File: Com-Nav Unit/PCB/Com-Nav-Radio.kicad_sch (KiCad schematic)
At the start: 91 parts, among them J1 USB_C_Receptacle_USB2.0_14P, Q10 SS8550, Q11 SS8550, Q12 SS8550, Q13 SS8550, Q14 SS8550, Q15 SS8550, Q16 SS8550, Q2 SS8550, Q3 SS8550, Q4 SS8550, Q5 SS8550, Q6 SS8550, Q7 SS8550, Q8 SS8550, Q9 SS8550, SW1 EC12D1524403, SW10 SW_Push, SW2 EC12E1240301, SW3 EC12D1524403, SW4 EC12E1240301, SW7 SW_Push, SW8 SW_Push, SW9 SW_Push, U1 STM32F411CEUx, U2 74HC595, U3 74HC595, U4 XC6206P332MR, Y2 25 MHz

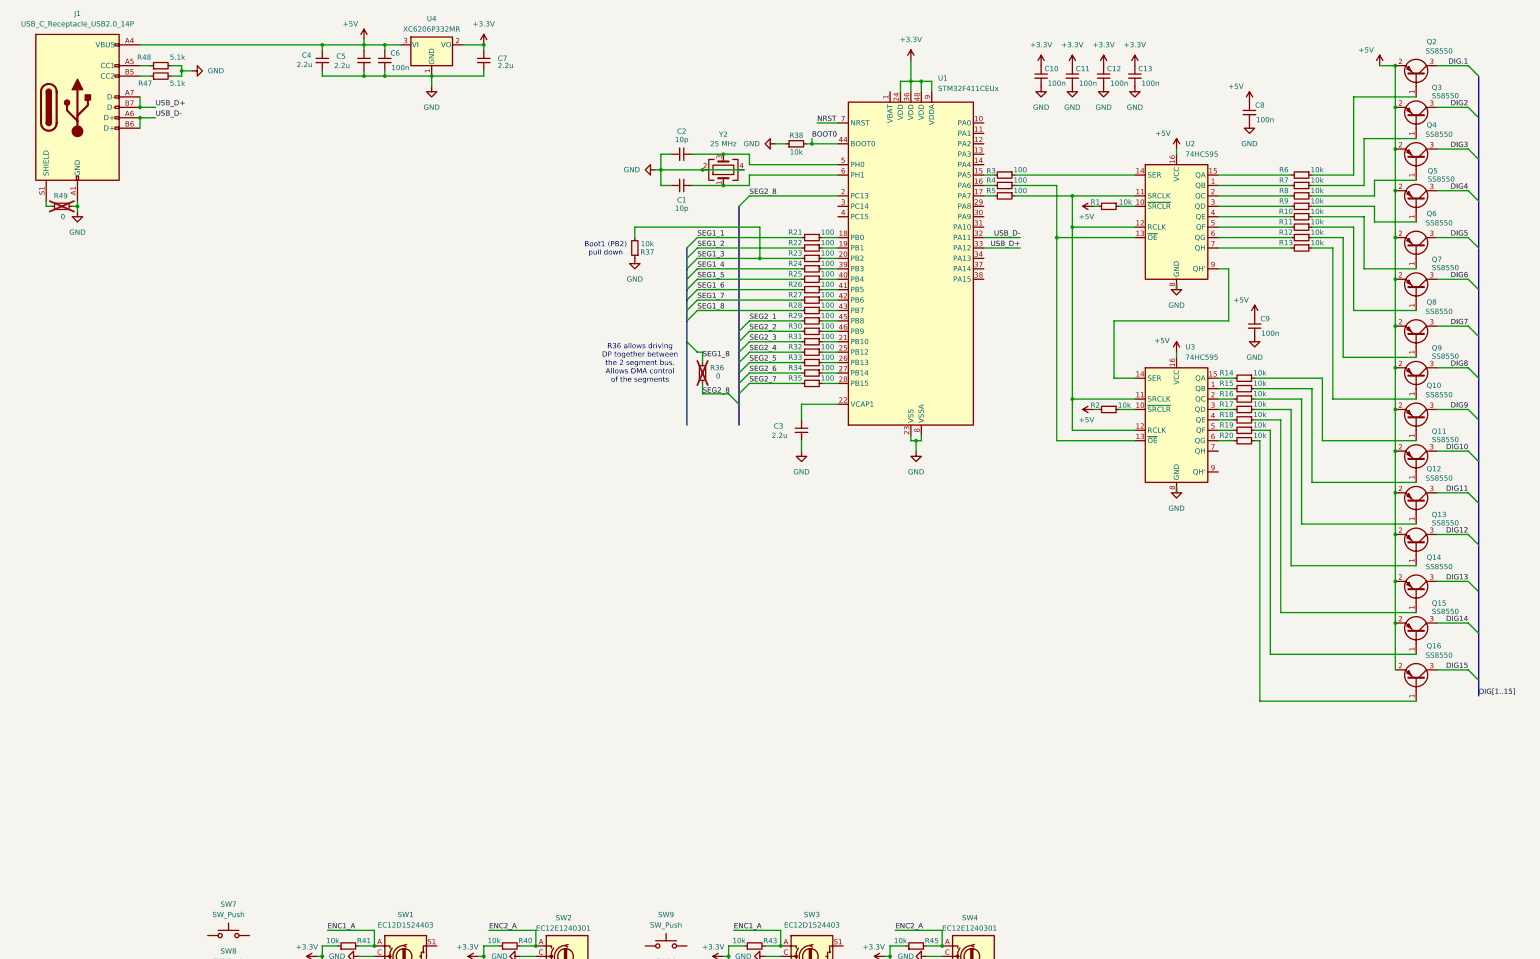
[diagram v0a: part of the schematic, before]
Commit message: PCB- Sch Connect 7 segments
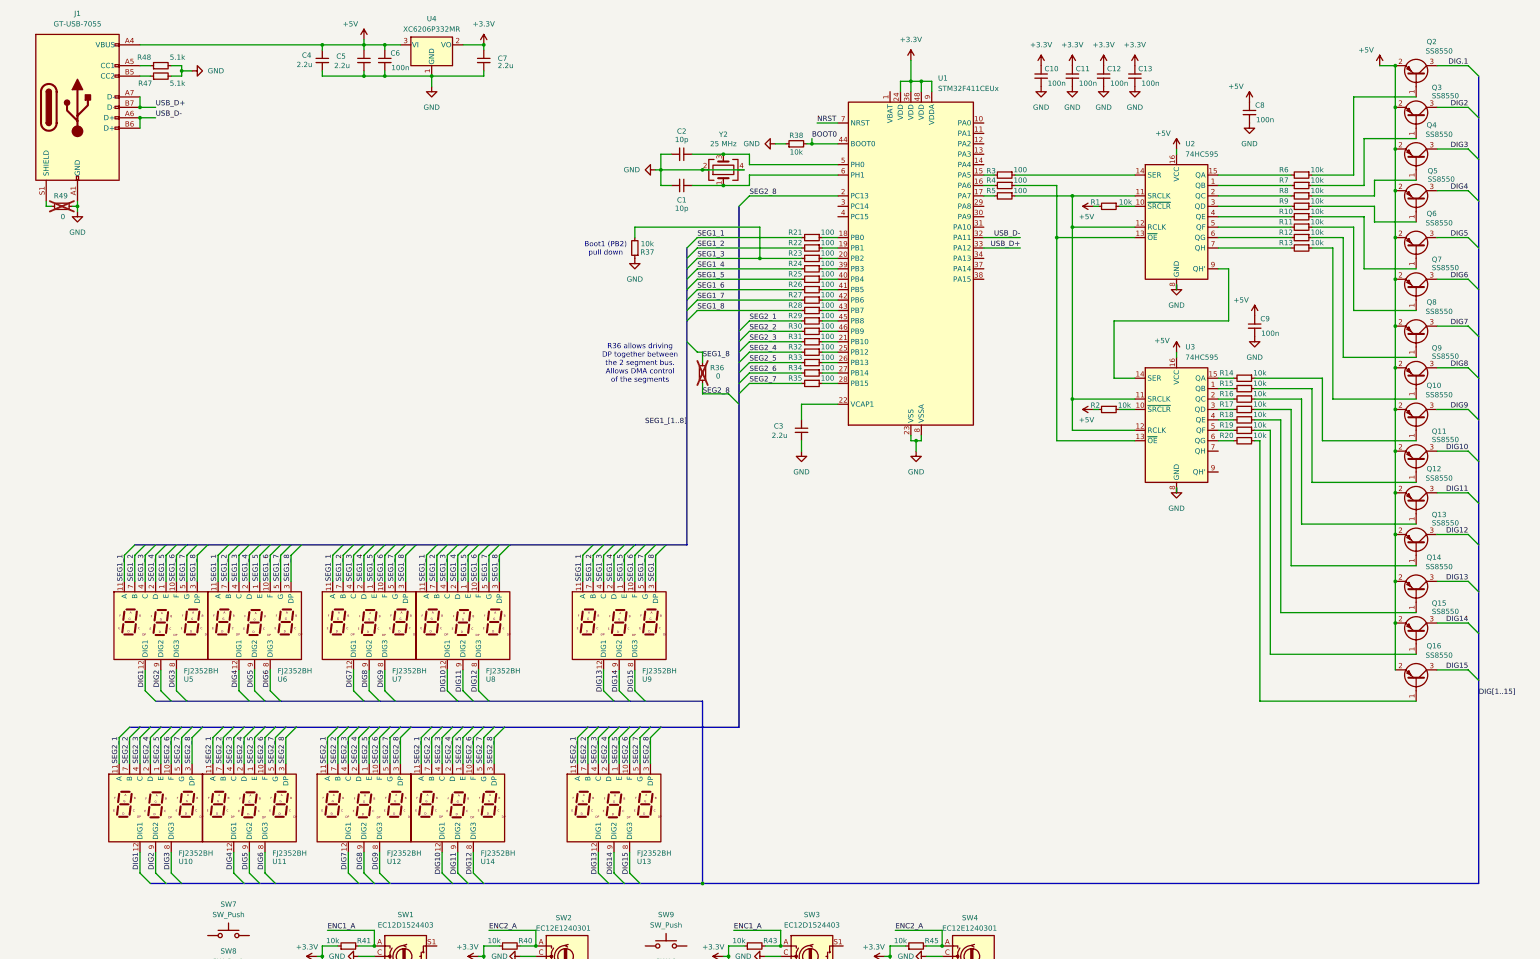
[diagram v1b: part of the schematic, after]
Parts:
- added U10, U11, U12, U13, U14, U5, U6, U7, U8, U9: FJ2352BH, Custom_7seg:FJ2352BH, symbol Custom_7seg:FJ2352BH
- J1: value USB_C_Receptacle_USB2.0_14P -> GT-USB-7055; footprint Connectors:USB_C_Receptacle_G-Switch_GT-USB-7051x -> Connectors:USB_C_Receptacle_G-Switch_GT-USB-7055x; PN (none) -> GT-USB-7055
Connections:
- net DIG10: now also U14.12 (DIG1), U8.12 (DIG1)
- net DIG11: now also U14.9 (DIG2), U8.9 (DIG2)
- net DIG12: now also U14.8 (DIG3), U8.8 (DIG3)
- net DIG13: now also U13.12 (DIG1), U9.12 (DIG1)
- net DIG14: now also U13.9 (DIG2), U9.9 (DIG2)
- net DIG15: now also U13.8 (DIG3), U9.8 (DIG3)
- net DIG2: now also U10.9 (DIG2), U5.9 (DIG2)
- net DIG3: now also U10.8 (DIG3), U5.8 (DIG3)
- net DIG4: now also U11.12 (DIG1), U6.12 (DIG1)
- net DIG5: now also U11.9 (DIG2), U6.9 (DIG2)
- net DIG6: now also U11.8 (DIG3), U6.8 (DIG3)
- net DIG7: now also U12.12 (DIG1), U7.12 (DIG1)
- net DIG8: now also U12.9 (DIG2), U7.9 (DIG2)
- net DIG9: now also U12.8 (DIG3), U7.8 (DIG3)
- net SEG1_1: now also U5.11 (A), U6.11 (A), U7.11 (A), U8.11 (A), U9.11 (A)
- net SEG1_2: now also U5.7 (B), U6.7 (B), U7.7 (B), U8.7 (B), U9.7 (B)
- net SEG1_3: now also U5.4 (C), U6.4 (C), U7.4 (C), U8.4 (C), U9.4 (C)
- net SEG1_4: now also U5.2 (D), U6.2 (D), U7.2 (D), U8.2 (D), U9.2 (D)
- net SEG1_5: now also U5.1 (E), U6.1 (E), U7.1 (E), U8.1 (E), U9.1 (E)
- net SEG1_6: now also U5.10 (F), U6.10 (F), U7.10 (F), U8.10 (F), U9.10 (F)
- net SEG1_7: now also U5.5 (G), U6.5 (G), U7.5 (G), U8.5 (G), U9.5 (G)
- net SEG1_8: now also U5.3 (DP), U6.3 (DP), U7.3 (DP), U8.3 (DP), U9.3 (DP)
- net SEG2_1: now also U10.11 (A), U11.11 (A), U12.11 (A), U13.11 (A), U14.11 (A)
- net SEG2_2: now also U10.7 (B), U11.7 (B), U12.7 (B), U13.7 (B), U14.7 (B)
- net SEG2_3: now also U10.4 (C), U11.4 (C), U12.4 (C), U13.4 (C), U14.4 (C)
- net SEG2_4: now also U10.2 (D), U11.2 (D), U12.2 (D), U13.2 (D), U14.2 (D)
- net SEG2_5: now also U10.1 (E), U11.1 (E), U12.1 (E), U13.1 (E), U14.1 (E)
- net SEG2_6: now also U10.10 (F), U11.10 (F), U12.10 (F), U13.10 (F), U14.10 (F)
- net SEG2_7: now also U10.5 (G), U11.5 (G), U12.5 (G), U13.5 (G), U14.5 (G)
- net SEG2_8: now also U10.3 (DP), U11.3 (DP), U12.3 (DP), U13.3 (DP), U14.3 (DP)
- new net DIG1: U10.12 (DIG1), U5.12 (DIG1)

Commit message: add swdio to stm in sch, add fab outputs to gitignore
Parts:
- U10, U11, U12, U13, U14, U5, U6, U7, U8, U9: PN (none) -> FJ2352BH
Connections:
- net SWDIO: now reaches U1.34 (PA13)
- net SWDCLK: now reaches U1.37 (PA14)
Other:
- moved on the sheet: J1, R47, R48, R49

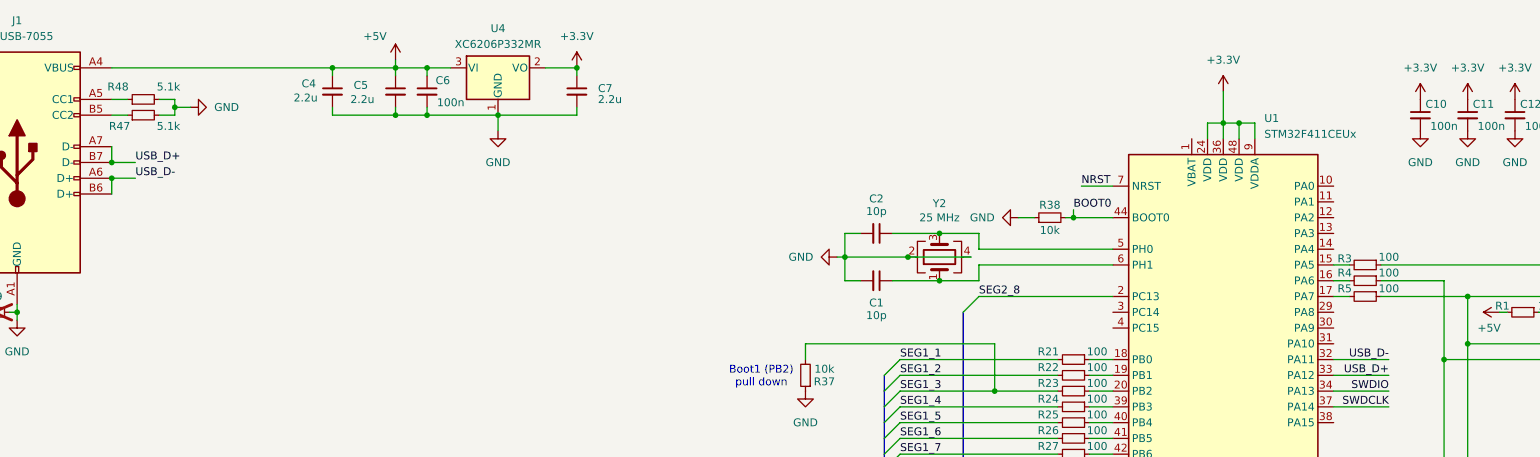
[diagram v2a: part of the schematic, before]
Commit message: PCB - Add ferite bead, connect encoders
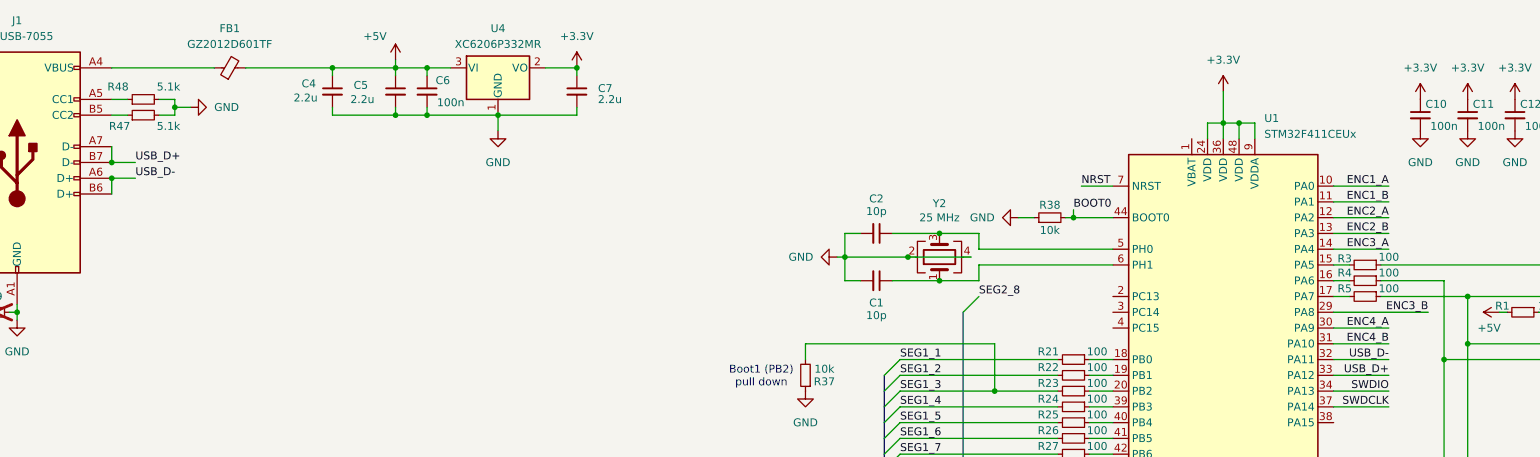
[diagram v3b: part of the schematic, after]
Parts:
- added FB1: GZ2012D601TF, Inductor_SMD:L_0805_2012Metric, symbol Device:FerriteBead_Small
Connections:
- net +5V: now also FB1.2; no longer J1.A4 (VBUS), J1.A9 (VBUS), J1.B4 (VBUS), J1.B9 (VBUS)
- net ENC1_A: now also U1.10 (PA0)
- net ENC1_B: now also U1.11 (PA1)
- net ENC2_A: now also U1.12 (PA2)
- net ENC2_B: now also U1.13 (PA3)
- net SEG2_8: no longer U1.2 (PC13)
- net ENC3_A: now reaches U1.14 (PA4)
- net ENC3_B: now reaches U1.29 (PA8)
- net ENC4_A: now reaches U1.30 (PA9)
- net ENC4_B: now reaches U1.31 (PA10)
- new net: FB1.1, J1.A4 (VBUS), J1.A9 (VBUS), J1.B4 (VBUS), J1.B9 (VBUS)
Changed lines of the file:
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@@
 	(wire
 		(pts
-			(xy 50.8 22.86) (xy 86.36 22.86)
-		)
-		(stroke
-			(width 0)
-			(type default)
-		)
-	)
-	(wire
-		(pts
 			(xy 73.66 180.34) (xy 73.66 175.26)
 		)
@@
 		)
 	)
+	(wire
+		(pts
+			(xy 256.54 49.53) (xy 247.65 49.53)
+		)
+		(stroke
+			(width 0)
+			(type default)
+		)
+	)
 	(bus
 		(pts
@@
 	(wire
 		(pts
-			(xy 190.5 59.69) (xy 212.09 59.69)
-		)
-		(stroke
-			(width 0)
-			(type default)
-		)
-	)
-	(wire
-		(pts
 			(xy 344.17 27.94) (xy 347.98 27.94)
 		)
@@
 	(wire
 		(pts
+			(xy 256.54 44.45) (xy 247.65 44.45)
+		)
+		(stroke
+			(width 0)
+			(type default)
+		)
+	)
+	(wire
+		(pts
 			(xy 226.06 252.73) (xy 237.49 252.73)
 		)
@@
 	(wire
 		(pts
+			(xy 262.89 62.23) (xy 247.65 62.23)
+		)
+		(stroke
+			(width 0)
+			(type default)
+		)
+	)
+	(wire
+		(pts
 			(xy 115.57 224.79) (xy 115.57 219.71)
 		)
@@
 	(wire
 		(pts
+			(xy 72.39 22.86) (xy 86.36 22.86)
+		)
+		(stroke
+			(width 0)
+			(type default)
+		)
+	)
+	(wire
+		(pts
 			(xy 208.28 80.01) (xy 212.09 80.01)
 		)
@@
 		)
 	)
+	(wire
+		(pts
+			(xy 256.54 67.31) (xy 247.65 67.31)
+		)
+		(stroke
+			(width 0)
+			(type default)
+		)
+	)
 	(bus
 		(pts
@@
 		)
 	)
+	(wire
+		(pts
+			(xy 256.54 41.91) (xy 247.65 41.91)
+		)
+		(stroke
+			(width 0)
+			(type default)
+		)
+	)
 	(bus
 		(pts
@@
 	(wire
 		(pts
+			(xy 256.54 52.07) (xy 247.65 52.07)
+		)
+		(stroke
+			(width 0)
+			(type default)
+		)
+	)
+	(wire
+		(pts
 			(xy 327.66 72.39) (xy 332.74 72.39)
 		)
@@
 		)
 	)
+	(wire
+		(pts
+			(xy 256.54 64.77) (xy 247.65 64.77)
+		)
+		(stroke
+			(width 0)
+			(type default)
+		)
+	)
 	(bus
 		(pts
@@
 	(wire
 		(pts
+			(xy 50.8 22.86) (xy 67.31 22.86)
+		)
+		(stroke
+			(width 0)
+			(type default)
+		)
+	)
+	(wire
+		(pts
 			(xy 186.69 252.73) (xy 198.12 252.73)
 		)
@@
 	(wire
 		(pts
+			(xy 256.54 46.99) (xy 247.65 46.99)
+		)
+		(stroke
+			(width 0)
+			(type default)
+		)
+	)
+	(wire
+		(pts
 			(xy 97.79 180.34) (xy 97.79 175.26)
 		)
@@
 		)
 	)
+	(label "ENC3_B"
+		(at 262.89 62.23 180)
+		(effects
+			(font
+				(size 1.27 1.27)
+			)
+			(justify right bottom)
+		)
+	)
 	(label "DIG1"
 		(at 43.18 175.26 270)
@@
 		)
 	)
+	(label "ENC3_A"
+		(at 256.54 52.07 180)
+		(effects
+			(font
+				(size 1.27 1.27)
+			)
+			(justify right bottom)
+		)
+	)
 	(label "DIG9"
 		(at 100.33 219.71 270)
@@
 		)
 	)
+	(label "ENC4_A"
+		(at 256.54 64.77 180)
+		(effects
+			(font
+				(size 1.27 1.27)
+			)
+			(justify right bottom)
+		)
+	)
 	(label "SEG2_3"
 		(at 115.57 198.12 90)
@@
 		)
 	)
+	(label "ENC1_A"
+		(at 256.54 41.91 180)
+		(effects
+			(font
+				(size 1.27 1.27)
+			)
+			(justify right bottom)
+		)
+	)
 	(label "DIG.1"
 		(at 365.76 27.94 180)
@@
 		)
 	)
+	(label "ENC4_B"
+		(at 256.54 67.31 180)
+		(effects
+			(font
+				(size 1.27 1.27)
+			)
+			(justify right bottom)
+		)
+	)
 	(label "DIG11"
 		(at 119.38 219.71 270)
@@
 		)
 	)
+	(label "ENC1_B"
+		(at 256.54 44.45 180)
+		(effects
+			(font
+				(size 1.27 1.27)
+			)
+			(justify right bottom)
+		)
+	)
 	(label "SEG1_1"
 		(at 88.9 153.67 90)
@@
 		)
 	)
+	(label "ENC2_B"
+		(at 256.54 49.53 180)
+		(effects
+			(font
+				(size 1.27 1.27)
+			)
+			(justify right bottom)
+		)
+	)
 	(label "SEG2_1"
 		(at 190.5 90.17 0)
@@
 		)
 	)
+	(label "ENC2_A"
+		(at 256.54 46.99 180)
+		(effects
+			(font
+				(size 1.27 1.27)
+			)
+			(justify right bottom)
+		)
+	)
 	(label "SEG1_3"
 		(at 93.98 153.67 90)
@@
 					(unit 1)
 				)
+			)
+		)
+	)
+	(symbol
+		(lib_id "Device:FerriteBead_Small")
+		(at 69.85 22.86 90)
+		(unit 1)
+		(exclude_from_sim no)
+		(in_bom yes)
+		(on_board yes)
+		(dnp no)
+		(fields_autoplaced yes)
+		(property "Reference" "FB1"
+			(at 69.8119 16.51 90)
+			(effects
+				(font
+					(size 1.27 1.27)
+				)
+			)
+		)
+		(property "Value" "GZ2012D601TF"
+			(at 69.8119 19.05 90)
+			(effects
+				(font
+					(size 1.27 1.27)
+				)
+			)
+		)
+		(property "Footprint" "Inductor_SMD:L_0805_2012Metric"
+			(at 69.85 24.638 90)
+			(effects
+				(font
+					(size 1.27 1.27)
+				)
+				(hide yes)
+			)
+		)
+		(property "Datasheet" "~"
+			(at 69.85 22.86 0)
+			(effects
+				(font
+					(size 1.27 1.27)
+				)
+				(hide yes)
+			)
+		)
+		(property "Description" "Ferrite bead, small symbol"
+			(at 69.85 22.86 0)
+			(effects
+				(font
+					(size 1.27 1.27)
+				)
+				(hide yes)
+			)
+		)
+		(property "PN" "GZ2012D601TF"
+			(at 69.85 22.86 90)
+			(effects
+				(font
+					(size 1.27 1.27)
+				)
+				(hide yes)
+			)
+		)
+		(pin "1"
+		)
+		(pin "2"
+		)
+		(instances
+			(project ""
+				(path "/69049761-9f2d-47f8-b9f8-414f51a5cecf"
+					(reference "FB1")
+					(unit 1)
+				)
